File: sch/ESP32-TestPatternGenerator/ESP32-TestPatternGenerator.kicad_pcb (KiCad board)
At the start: 2 copper layers, 43.2 x 68.6 mm, 8 parts

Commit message: finalised PCB
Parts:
- renumbered Format to PAL/NTSC
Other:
- board text added: "ESP32-TestPatternGenerator v1.0 - 2024 nmur"

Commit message: added v1.0 gerber
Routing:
- net Net-(LOLIND32-IO2): track 46.8 -> 53.3 mm
- net Net-(LOLIND32-IO15): track 54.9 -> 61.4 mm
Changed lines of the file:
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@@
   (segment (start 99.06 81.28) (end 99.06 109.22) (width 0.5) (layer "B.Cu") (net 1))
   (segment (start 99.06 109.22) (end 96.52 111.76) (width 0.5) (layer "B.Cu") (net 1))
+  (segment (start 116.84 81.28) (end 116.84 74.78) (width 0.5) (layer "B.Cu") (net 31))
   (segment (start 116.84 124.46) (end 119.38 127) (width 0.5) (layer "B.Cu") (net 31))
   (segment (start 116.84 81.28) (end 116.84 124.46) (width 0.5) (layer "B.Cu") (net 31))
   (segment (start 106.97 81.28) (end 114.3 88.61) (width 0.5) (layer "B.Cu") (net 32))
   (segment (start 114.3 127) (end 116.84 129.54) (width 0.5) (layer "B.Cu") (net 32))
+  (segment (start 106.97 81.28) (end 106.97 74.78) (width 0.5) (layer "B.Cu") (net 32))
   (segment (start 114.3 88.61) (end 114.3 127) (width 0.5) (layer "B.Cu") (net 32))
   (segment (start 116.84 129.54) (end 119.38 129.54) (width 0.5) (layer "B.Cu") (net 32))

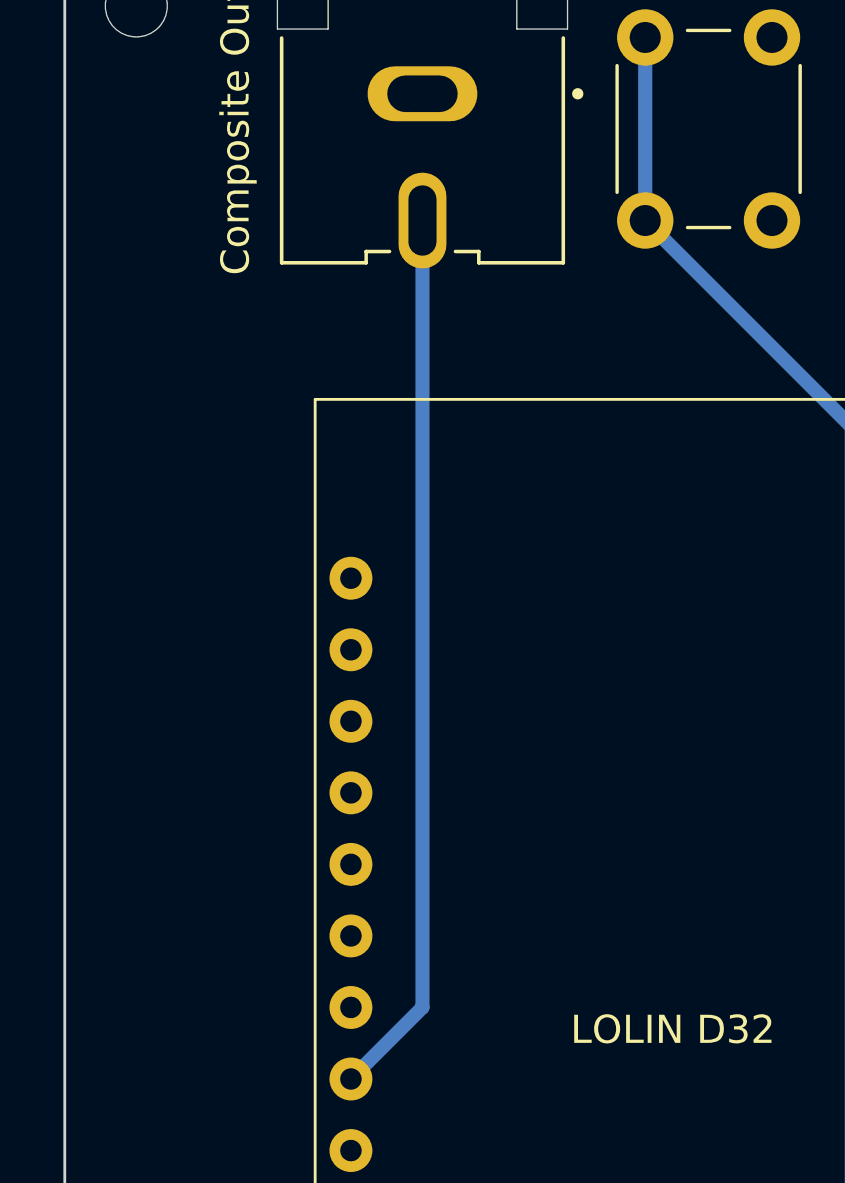
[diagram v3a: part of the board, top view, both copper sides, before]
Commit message: increased composite pin hole clearance
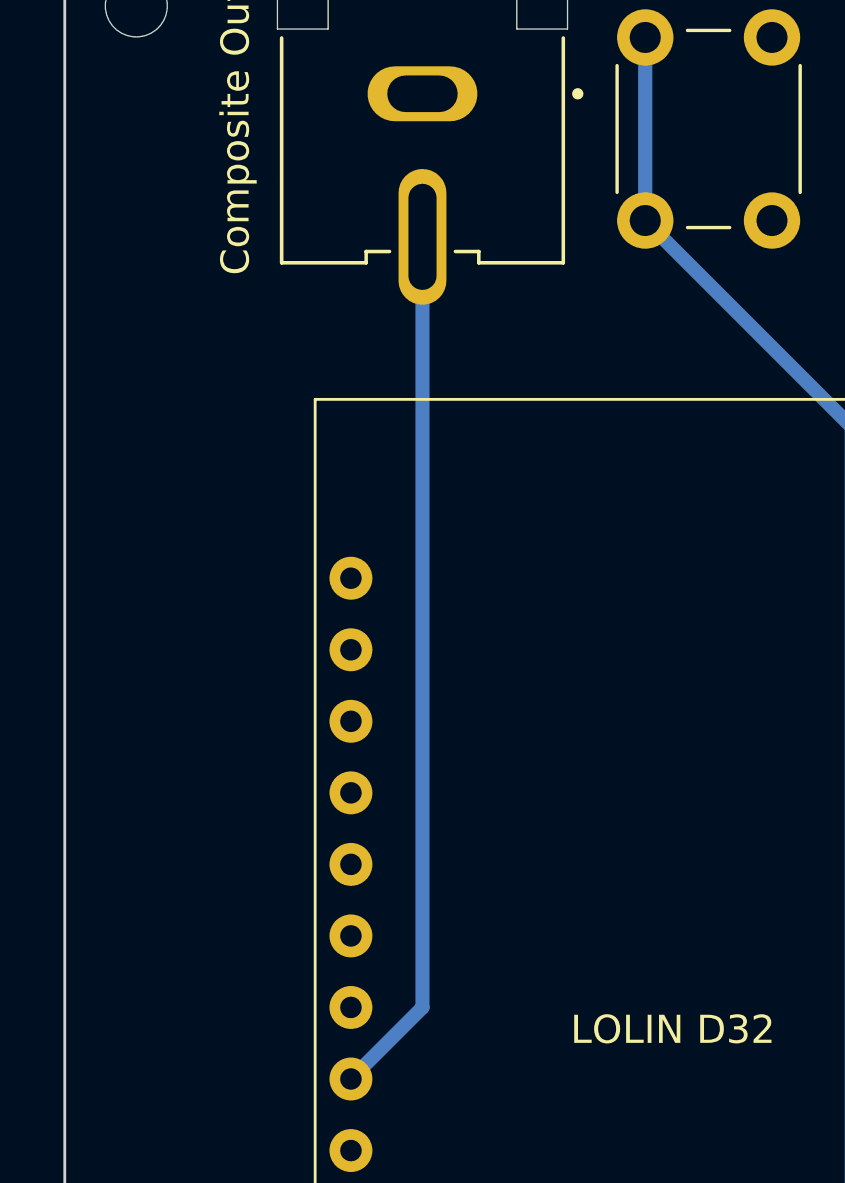
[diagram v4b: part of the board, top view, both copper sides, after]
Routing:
- net Net-(J1-In): track 31.5 -> 31.0 mm
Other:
- board text added: "ESP32-TestPatternGenerator v1.1 - 2024 nmur"
- board text removed: "ESP32-TestPatternGenerator v1.0 - 2024 nmur"

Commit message: added JLCPCB order number marker and USB positioning aid labels on silkscreen
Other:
- board text added: "JLCJLCJLCJLC"
- board text added: "USB"
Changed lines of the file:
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@@
       (net 18 "unconnected-(LOLIND32-GND-Pad17)") (pinfunction "Ext") (pintype "passive") (solder_mask_margin 0.102))
   )
+  (gr_rect (start 110.49 134.62) (end 116.84 139.7)
+    (stroke (width 0.15) (type default)) (fill none) (layer "F.SilkS"))
   (gr_arc (start 87.63 139.7) (mid 86.731974 139.328026) (end 86.36 138.43)
     (stroke (width 0.1) (type default)) (layer "Edge.Cuts"))
@@
     )
   )
+  (gr_text "JLCJLCJLCJLC" (at 101.6 119.38 90) (layer "F.SilkS")
+    (effects (font (size 1 1) (thickness 0.15)) (justify left bottom))
+  )
+  (gr_text "USB" (at 112.014 133.858) (layer "F.SilkS")
+    (effects (font (size 1 1) (thickness 0.15)) (justify left bottom))
+  )
   (segment (start 99.06 81.86) (end 99.06 109.22) (width 0.5) (layer "B.Cu") (net 1))
